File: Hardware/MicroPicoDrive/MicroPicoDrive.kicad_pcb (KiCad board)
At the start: 2 copper layers, 66 x 59 mm, 16 parts, among them IC1 SN74LVC1T45DBVR, IC2 SN74LVC1T45DBVR, IC3 TXU0304QPWRQ1, J1 Conn_02x16, J2 QL_CONN, U1 LM7805_TO220, U2 Pico

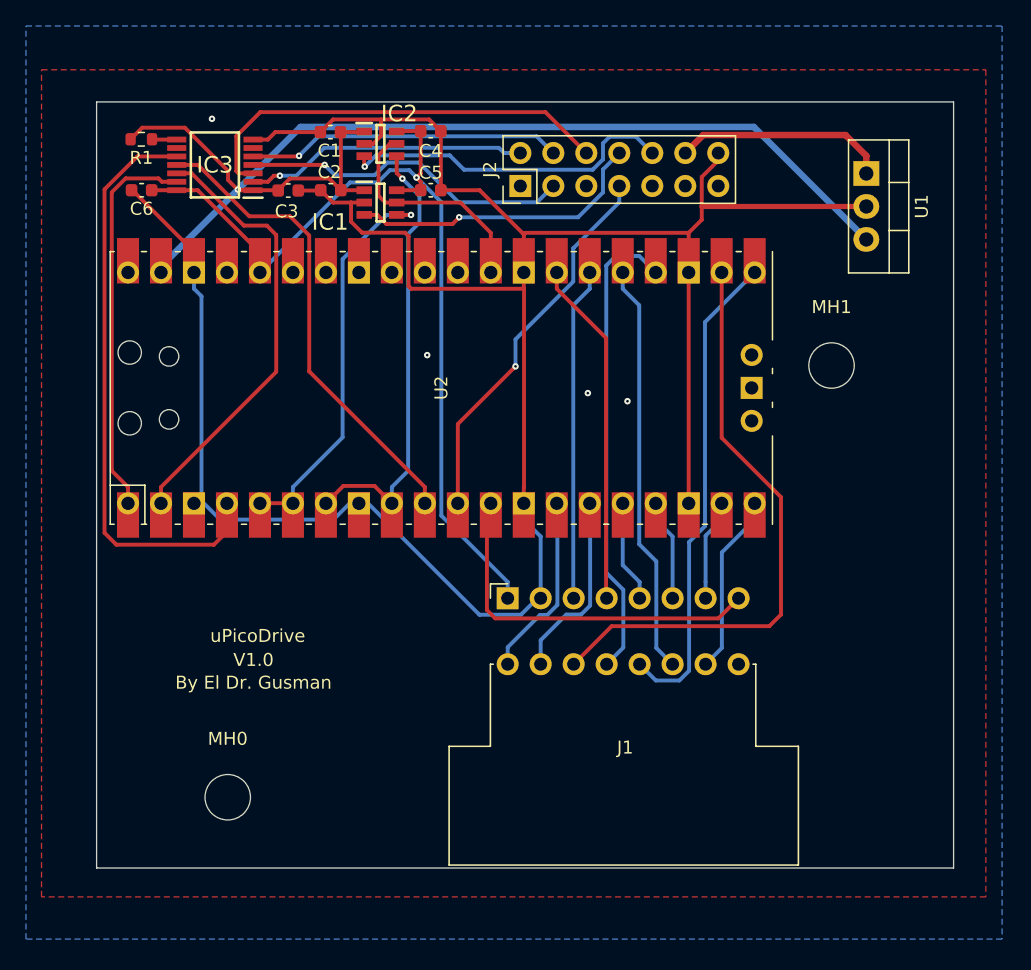
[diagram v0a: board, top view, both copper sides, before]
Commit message: Updated PCB, added BOM and links, updated MDToolsUI
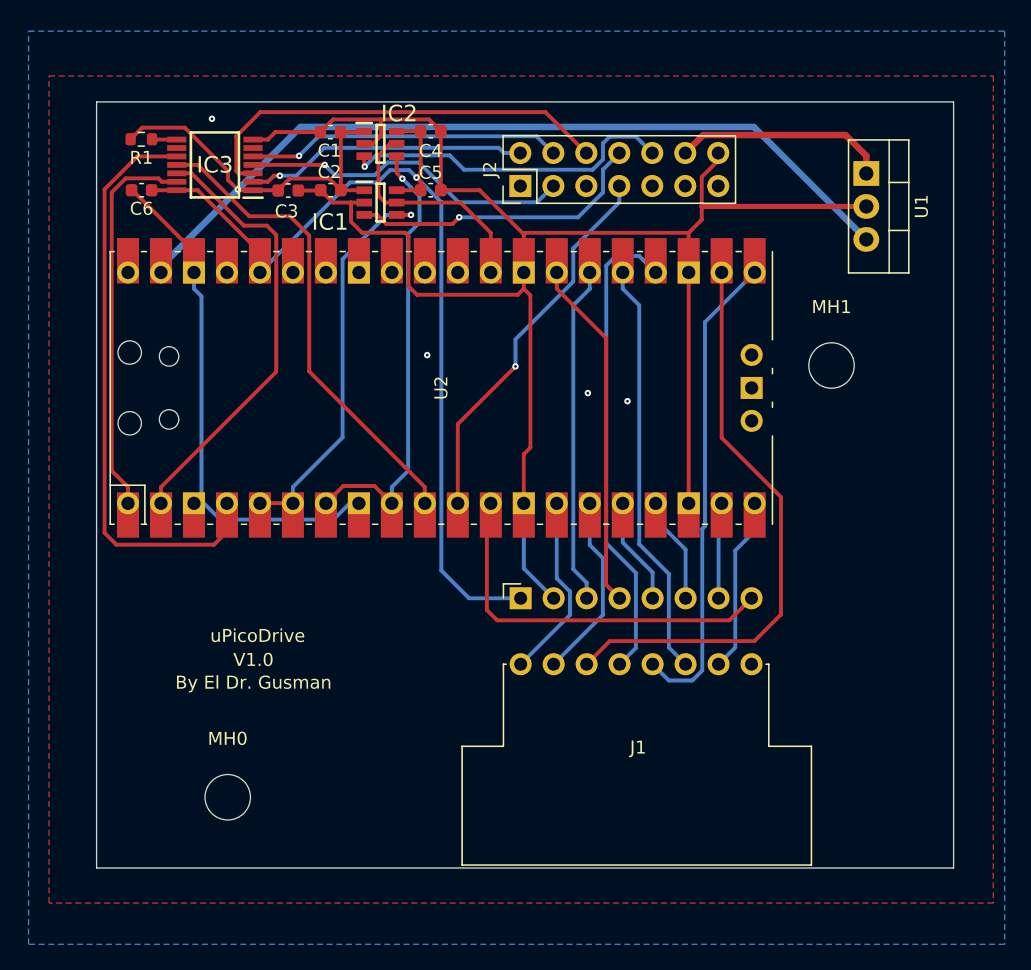
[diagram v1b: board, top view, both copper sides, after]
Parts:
- moved J1 1.00 mm to (155.8, 121.9)
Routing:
- net GND: track 195.7 -> 178.7 mm
- net +3V3: track 71.0 -> 73.8 mm
- net /UI_LD_SELECT: track 28.6 -> 29.8 mm
- net /UI_SD_CS: track 45.8 -> 44.8 mm

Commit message: Updated PCBs
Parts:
- moved MH0 1.33 mm to (125.6, 125.7)
- moved MH1 1.33 mm to (172.1, 92.1)
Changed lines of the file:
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@@
       (psa4output false)
       (plotreference true)
-      (plotvalue true)
+      (plotvalue false)
       (plotinvisibletext false)
       (sketchpadsonfab false)
@@
       (drillshape 0)
       (scaleselection 1)
-      (outputdirectory "Fabrication/")
+      (outputdirectory "Fabrication_2/")
     )
   )
@@
   )
   (footprint "MountingHole:MountingHole_3.5mm" (layer "F.Cu")
-    (at 124.315 125.7)
+    (at 125.645 125.7)
     (descr "Mounting Hole 3.5mm, no annular")
     (tags "mounting hole 3.5mm no annular")
@@
   )
   (footprint "MountingHole:MountingHole_3.5mm" (layer "F.Cu")
-    (at 170.815 92.45)
+    (at 172.1 92.125)
     (descr "Mounting Hole 3.5mm, no annular")
     (tags "mounting hole 3.5mm no annular")
